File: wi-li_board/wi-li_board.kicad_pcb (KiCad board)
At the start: 2 copper layers, 100 x 100 mm, 96 parts, among them J1 Barrel_Jack_MountingPin, J2 XT30, J3 XT30, J4 XT30, J5 DBG, Q1 Q_NMOS_DGS, Q2 Q_NMOS_DGS, Q3 Q_NMOS_DGS, U1 AP1509, U2 ESP-12E, U3 ADS1115IDGS

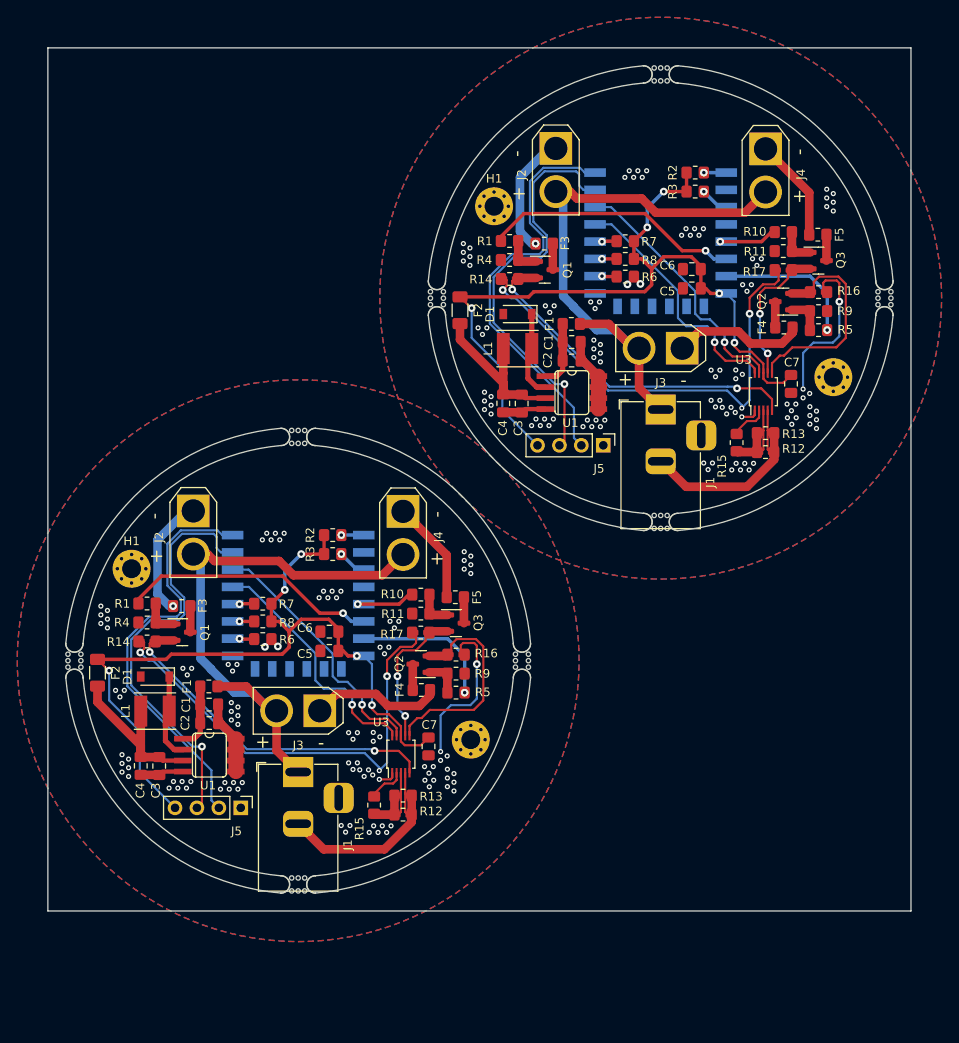
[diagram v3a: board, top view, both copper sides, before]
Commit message: use 2x5mm mouse bites
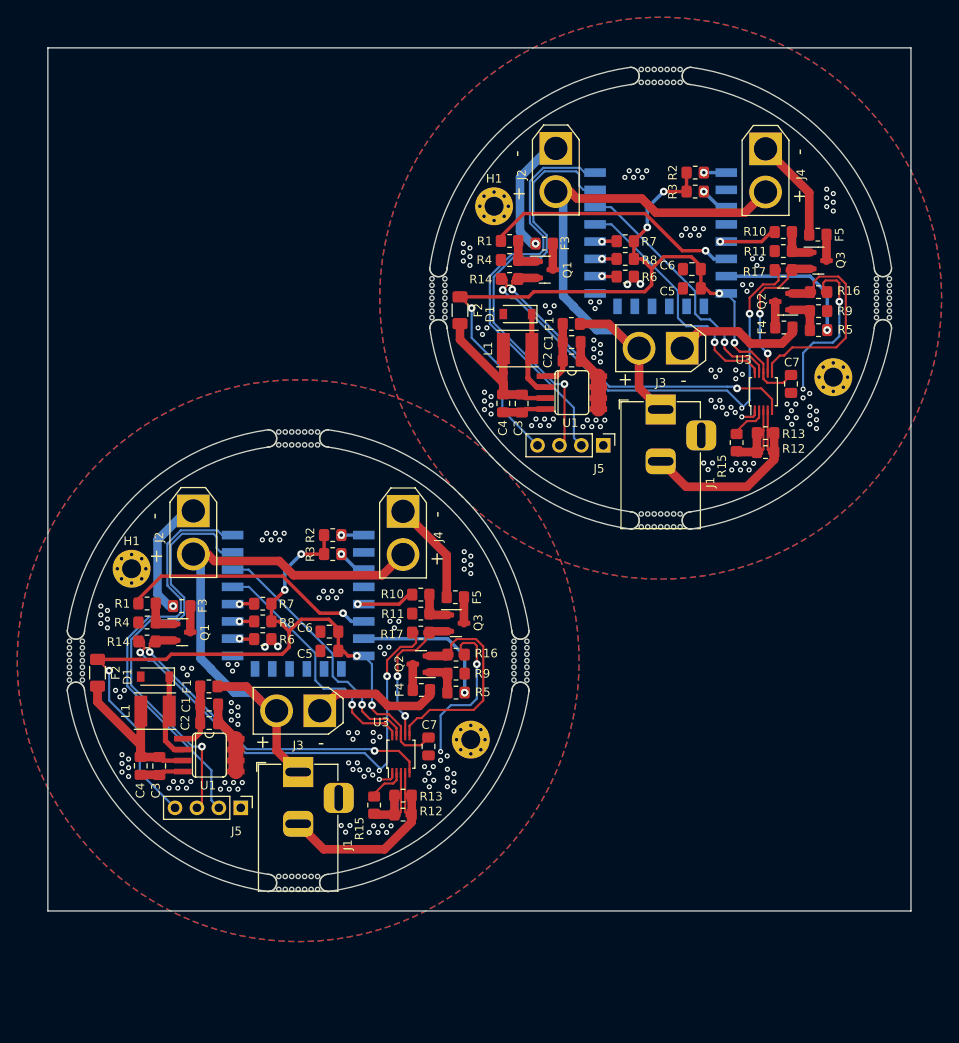
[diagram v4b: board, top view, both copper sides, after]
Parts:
- removed mouse-bite-2mm-slot (x8): VAL**, Panelization:mouse-bite-2mm-slot
- added mouse-bite-2x5mm: VAL**, Misc:mouse-bite-2x5mm, F.Cu at (197.2, 82.0)
- added mouse-bite-2x5mm: VAL**, Misc:mouse-bite-2x5mm, F.Cu at (129.5, 98.2)
- added mouse-bite-2x5mm: VAL**, Misc:mouse-bite-2x5mm, F.Cu at (197.2, 30.5)
- added mouse-bite-2x5mm: VAL**, Misc:mouse-bite-2x5mm, F.Cu at (155.2, 124.0)
- added mouse-bite-2x5mm: VAL**, Misc:mouse-bite-2x5mm, F.Cu at (155.2, 72.5)
- added mouse-bite-2x5mm: VAL**, Misc:mouse-bite-2x5mm, F.Cu at (171.5, 56.2)
- added mouse-bite-2x5mm: VAL**, Misc:mouse-bite-2x5mm, F.Cu at (181.0, 98.2)
- added mouse-bite-2x5mm: VAL**, Misc:mouse-bite-2x5mm, F.Cu at (223.0, 56.2)
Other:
- outline, holes or cut-outs redrawn
